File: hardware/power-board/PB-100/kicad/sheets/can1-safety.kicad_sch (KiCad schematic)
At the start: 2 parts

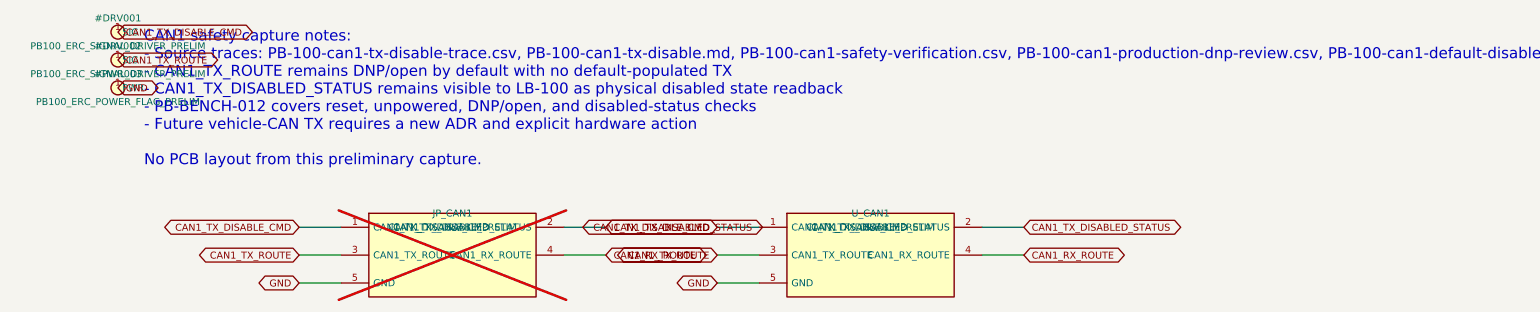
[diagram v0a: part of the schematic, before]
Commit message: Remediate PB footprint pad mapping
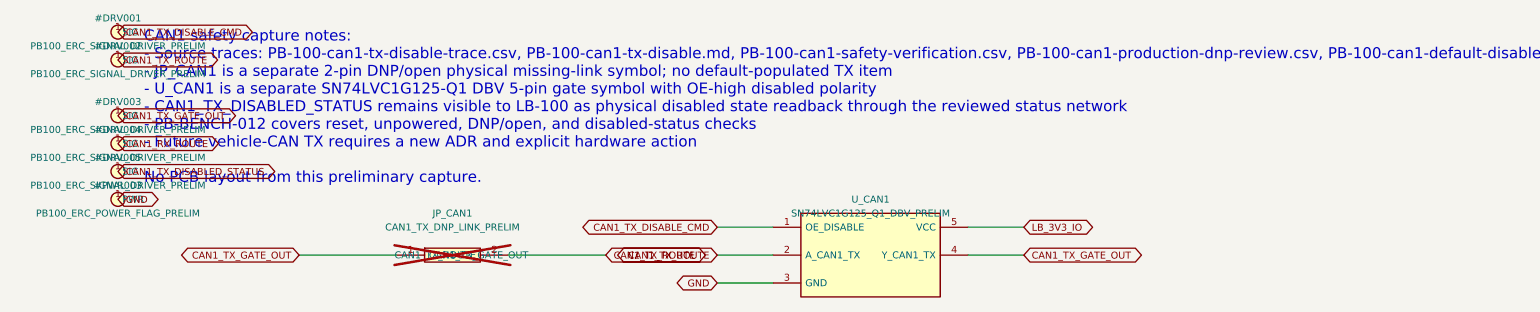
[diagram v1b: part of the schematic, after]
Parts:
- JP_CAN1: value CAN1_TX_DISABLE_PRELIM -> CAN1_TX_DNP_LINK_PRELIM; symbol PB100:PB100_CAN1_TX_DISABLE_PRELIM -> PB100:PB100_CAN1_TX_DNP_LINK_PRELIM
- U_CAN1: value CAN1_TX_DISABLE_PRELIM -> SN74LVC1G125_Q1_DBV_PRELIM; symbol PB100:PB100_CAN1_TX_DISABLE_PRELIM -> PB100:PB100_SN74LVC1G125_Q1_DBV_PRELIM
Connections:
- net CAN1_RX_ROUTE: no longer JP_CAN1.4 (CAN1_RX_ROUTE), U_CAN1.4 (CAN1_RX_ROUTE)
- net CAN1_TX_DISABLED_STATUS: no longer JP_CAN1.2 (CAN1_TX_DISABLED_STATUS), U_CAN1.2 (CAN1_TX_DISABLED_STATUS)
- net CAN1_TX_DISABLE_CMD: no longer JP_CAN1.1 (CAN1_TX_DISABLE_CMD)
- net CAN1_TX_ROUTE: now also JP_CAN1.2 (CAN1_TX_ROUTE), U_CAN1.2 (A_CAN1_TX); no longer JP_CAN1.3 (CAN1_TX_ROUTE), U_CAN1.3 (CAN1_TX_ROUTE)
- net GND: now also U_CAN1.3 (GND); no longer JP_CAN1.5 (GND), U_CAN1.5 (GND)
- new net CAN1_TX_GATE_OUT: JP_CAN1.1 (CAN1_TX_GATE_OUT), U_CAN1.4 (Y_CAN1_TX)
- new net LB_3V3_IO: U_CAN1.5 (VCC)

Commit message: fix
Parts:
- added R_CAN1_OE, R_CAN1_TX_BIAS: 47k 1%, PB100:R0402, symbol PB100:PB100_CAN1_SAFETY_RESISTOR_PRELIM
- added R_CAN1_STATUS_PULL: 100k 1%, PB100:R0402, symbol PB100:PB100_CAN1_SAFETY_RESISTOR_PRELIM
- added R_CAN1_STATUS_SER: 1k 1%, PB100:R0402, symbol PB100:PB100_CAN1_SAFETY_RESISTOR_PRELIM
- JP_CAN1: footprint (none) -> PB100:R0603_DNP_LINK_1608Metric
- U_CAN1: footprint (none) -> PB100:SOT-23-5_DBV_TI
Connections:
- net CAN1_TX_DISABLED_STATUS: now also R_CAN1_STATUS_PULL.2 (B), R_CAN1_STATUS_SER.2 (B)
- net CAN1_TX_DISABLE_CMD: now also R_CAN1_OE.2 (B), R_CAN1_STATUS_SER.1 (A)
- net CAN1_TX_ROUTE: no longer JP_CAN1.2 (CAN1_TX_ROUTE)
- net LB_3V3_IO: now also R_CAN1_OE.1 (A), R_CAN1_STATUS_PULL.1 (A), R_CAN1_TX_BIAS.1 (A)
- new net CAN1_TXD_SAFE: JP_CAN1.2 (CAN1_TXD_SAFE), R_CAN1_TX_BIAS.2 (B)
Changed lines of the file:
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@@
     (property "Reference" "JP_CAN1" (at 76.20 53.34 0) (effects (font (size 1.27 1.27))))
     (property "Value" "CAN1_TX_DNP_LINK_PRELIM" (at 76.20 55.88 0) (effects (font (size 1.27 1.27))))
-    (property "Footprint" "" (at 76.20 66.04 0) (effects (font (size 1.27 1.27)) hide))
+    (property "Footprint" "PB100:R0603_DNP_LINK_1608Metric" (at 76.20 66.04 0) (effects (font (size 1.27 1.27)) hide))
     (property "Datasheet" "../PB-100-can1-tx-disable.md" (at 76.20 68.58 0) (effects (font (size 1.27 1.27)) hide))
     (pin "1")
@@
   (global_label "CAN1_TX_GATE_OUT" (shape bidirectional) (at 48.26 60.96 0) (fields_autoplaced) (effects (font (size 1.27 1.27)) (justify right)) (property "Intersheetrefs" "${INTERSHEET_REFS}" (at 48.26 60.96 0) (effects (font (size 1.27 1.27)) hide)))
   (wire (pts (xy 86.36 60.96) (xy 104.14 60.96)) (stroke (width 0) (type default)))
-  (global_label "CAN1_TX_ROUTE" (shape bidirectional) (at 104.14 60.96 0) (fields_autoplaced) (effects (font (size 1.27 1.27)) (justify left)) (property "Intersheetrefs" "${INTERSHEET_REFS}" (at 104.14 60.96 0) (effects (font (size 1.27 1.27)) hide)))
+  (global_label "CAN1_TXD_SAFE" (shape bidirectional) (at 104.14 60.96 0) (fields_autoplaced) (effects (font (size 1.27 1.27)) (justify left)) (property "Intersheetrefs" "${INTERSHEET_REFS}" (at 104.14 60.96 0) (effects (font (size 1.27 1.27)) hide)))
   (symbol
     (lib_id "PB100:PB100_SN74LVC1G125_Q1_DBV_PRELIM")
@@
     (property "Reference" "U_CAN1" (at 152.40 50.80 0) (effects (font (size 1.27 1.27))))
     (property "Value" "SN74LVC1G125_Q1_DBV_PRELIM" (at 152.40 53.34 0) (effects (font (size 1.27 1.27))))
-    (property "Footprint" "" (at 152.40 71.12 0) (effects (font (size 1.27 1.27)) hide))
+    (property "Footprint" "PB100:SOT-23-5_DBV_TI" (at 152.40 71.12 0) (effects (font (size 1.27 1.27)) hide))
     (property "Datasheet" "https://www.ti.com/lit/ds/symlink/sn74lvc1g125-q1.pdf" (at 152.40 73.66 0) (effects (font (size 1.27 1.27)) hide))
     (pin "1")
@@
   (global_label "LB_3V3_IO" (shape bidirectional) (at 180.34 55.88 0) (fields_autoplaced) (effects (font (size 1.27 1.27)) (justify left)) (property "Intersheetrefs" "${INTERSHEET_REFS}" (at 180.34 55.88 0) (effects (font (size 1.27 1.27)) hide)))
   (symbol
+    (lib_id "PB100:PB100_CAN1_SAFETY_RESISTOR_PRELIM")
+    (at 76.20 91.44 0)
+    (unit 1)
+    (exclude_from_sim no)
+    (in_bom yes)
+    (on_board yes)
+    (dnp no)
+    (property "Reference" "R_CAN1_OE" (at 76.20 86.36 0) (effects (font (size 1.27 1.27))))
+    (property "Value" "47k 1%" (at 76.20 88.90 0) (effects (font (size 1.27 1.27))))
+    (property "Footprint" "PB100:R0402" (at 76.20 96.52 0) (effects (font (size 1.27 1.27)) hide))
+    (property "Datasheet" "../PB-100-can1-tx-disable-design-calculation.md" (at 76.20 99.06 0) (effects (font (size 1.27 1.27)) hide))
+    (pin "1")
+    (pin "2")
+    (instances
+      (project "PB-100"
+        (path "/1af68b81-10b0-5461-9124-39421a2a6932/80055f99-6297-4ce2-96ea-d333e2a69a50/"
+          (reference "R_CAN1_OE")
+          (unit 1)
+        )
+      )
+    )
+  )
+  (global_label "LB_3V3_IO" (shape bidirectional) (at 68.58 91.44 0) (fields_autoplaced) (effects (font (size 1.27 1.27)) (justify right)) (property "Intersheetrefs" "${INTERSHEET_REFS}" (at 68.58 91.44 0) (effects (font (size 1.27 1.27)) hide)))
+  (global_label "CAN1_TX_DISABLE_CMD" (shape bidirectional) (at 83.82 91.44 0) (fields_autoplaced) (effects (font (size 1.27 1.27)) (justify left)) (property "Intersheetrefs" "${INTERSHEET_REFS}" (at 83.82 91.44 0) (effects (font (size 1.27 1.27)) hide)))
+  (symbol
+    (lib_id "PB100:PB100_CAN1_SAFETY_RESISTOR_PRELIM")
+    (at 127.00 91.44 0)
+    (unit 1)
+    (exclude_from_sim no)
+    (in_bom yes)
+    (on_board yes)
+    (dnp no)
+    (property "Reference" "R_CAN1_TX_BIAS" (at 127.00 86.36 0) (effects (font (size 1.27 1.27))))
+    (property "Value" "47k 1%" (at 127.00 88.90 0) (effects (font (size 1.27 1.27))))
+    (property "Footprint" "PB100:R0402" (at 127.00 96.52 0) (effects (font (size 1.27 1.27)) hide))
+    (property "Datasheet" "../PB-100-can1-tx-disable-design-calculation.md" (at 127.00 99.06 0) (effects (font (size 1.27 1.27)) hide))
+    (pin "1")
+    (pin "2")
+    (instances
+      (project "PB-100"
+        (path "/1af68b81-10b0-5461-9124-39421a2a6932/8b75beab-22de-42a1-ba89-68e9bd2ad844/"
+          (reference "R_CAN1_TX_BIAS")
+          (unit 1)
+        )
+      )
+    )
+  )
+  (global_label "LB_3V3_IO" (shape bidirectional) (at 119.38 91.44 0) (fields_autoplaced) (effects (font (size 1.27 1.27)) (justify right)) (property "Intersheetrefs" "${INTERSHEET_REFS}" (at 119.38 91.44 0) (effects (font (size 1.27 1.27)) hide)))
+  (global_label "CAN1_TXD_SAFE" (shape bidirectional) (at 134.62 91.44 0) (fields_autoplaced) (effects (font (size 1.27 1.27)) (justify left)) (property "Intersheetrefs" "${INTERSHEET_REFS}" (at 134.62 91.44 0) (effects (font (size 1.27 1.27)) hide)))
+  (symbol
+    (lib_id "PB100:PB100_CAN1_SAFETY_RESISTOR_PRELIM")
+    (at 76.20 116.84 0)
+    (unit 1)
+    (exclude_from_sim no)
+    (in_bom yes)
+    (on_board yes)
+    (dnp no)
+    (property "Reference" "R_CAN1_STATUS_SER" (at 76.20 111.76 0) (effects (font (size 1.27 1.27))))
+    (property "Value" "1k 1%" (at 76.20 114.30 0) (effects (font (size 1.27 1.27))))
+    (property "Footprint" "PB100:R0402" (at 76.20 121.92 0) (effects (font (size 1.27 1.27)) hide))
+    (property "Datasheet" "../PB-100-can1-tx-disable-design-calculation.md" (at 76.20 124.46 0) (effects (font (size 1.27 1.27)) hide))
+    (pin "1")
+    (pin "2")
+    (instances
+      (project "PB-100"
+        (path "/1af68b81-10b0-5461-9124-39421a2a6932/32b2e633-ddfb-4068-9ee8-5caed1060666/"
+          (reference "R_CAN1_STATUS_SER")
+          (unit 1)
+        )
+      )
+    )
+  )
+  (global_label "CAN1_TX_DISABLE_CMD" (shape bidirectional) (at 68.58 116.84 0) (fields_autoplaced) (effects (font (size 1.27 1.27)) (justify right)) (property "Intersheetrefs" "${INTERSHEET_REFS}" (at 68.58 116.84 0) (effects (font (size 1.27 1.27)) hide)))
+  (global_label "CAN1_TX_DISABLED_STATUS" (shape bidirectional) (at 83.82 116.84 0) (fields_autoplaced) (effects (font (size 1.27 1.27)) (justify left)) (property "Intersheetrefs" "${INTERSHEET_REFS}" (at 83.82 116.84 0) (effects (font (size 1.27 1.27)) hide)))
+  (symbol
+    (lib_id "PB100:PB100_CAN1_SAFETY_RESISTOR_PRELIM")
+    (at 127.00 116.84 0)
+    (unit 1)
+    (exclude_from_sim no)
+    (in_bom yes)
+    (on_board yes)
+    (dnp no)
+    (property "Reference" "R_CAN1_STATUS_PULL" (at 127.00 111.76 0) (effects (font (size 1.27 1.27))))
+    (property "Value" "100k 1%" (at 127.00 114.30 0) (effects (font (size 1.27 1.27))))
+    (property "Footprint" "PB100:R0402" (at 127.00 121.92 0) (effects (font (size 1.27 1.27)) hide))
+    (property "Datasheet" "../PB-100-can1-tx-disable-design-calculation.md" (at 127.00 124.46 0) (effects (font (size 1.27 1.27)) hide))
+    (pin "1")
+    (pin "2")
+    (instances
+      (project "PB-100"
+        (path "/1af68b81-10b0-5461-9124-39421a2a6932/ac9557eb-9bb9-41f8-b23a-db6800c089e1/"
+          (reference "R_CAN1_STATUS_PULL")
+          (unit 1)
+        )
+      )
+    )
+  )
+  (global_label "LB_3V3_IO" (shape bidirectional) (at 119.38 116.84 0) (fields_autoplaced) (effects (font (size 1.27 1.27)) (justify right)) (property "Intersheetrefs" "${INTERSHEET_REFS}" (at 119.38 116.84 0) (effects (font (size 1.27 1.27)) hide)))
+  (global_label "CAN1_TX_DISABLED_STATUS" (shape bidirectional) (at 134.62 116.84 0) (fields_autoplaced) (effects (font (size 1.27 1.27)) (justify left)) (property "Intersheetrefs" "${INTERSHEET_REFS}" (at 134.62 116.84 0) (effects (font (size 1.27 1.27)) hide)))
+  (symbol
     (lib_id "PB100:PB100_ERC_SIGNAL_DRIVER_PRELIM")

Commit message: feat(hardware): accept CAN1 and 80V freeze decisions
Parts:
- added C_CAN1_VCC, C_CAN1_VIO: 100nF 50V X7R, PB100:C0402, symbol PB100:PB100_CAN1_DECOUPLING_CAP
- added D_CAN1: ESD2CANFD24QDBZRQ1, PB100:SOT-23-3_DBZ_TI, symbol PB100:PB100_ESD2CANFD24_Q1_PRELIM
- added JP_CAN1_NORMAL: CAN1_NORMAL_MODE_DNP, PB100:R0603_DNP_LINK_1608Metric, symbol PB100:PB100_CAN1_TX_DNP_LINK_PRELIM
- added R_CAN1_SILENT: 47k 1%, PB100:R0402, symbol PB100:PB100_CAN1_SAFETY_RESISTOR_PRELIM
- added R_CAN1_TERM: 120R 1% DNP, PB100:R0603_DNP_LINK_1608Metric, symbol PB100:PB100_CAN1_SAFETY_RESISTOR_PRELIM
- added U_CAN1_PHY: TJA1051TK/3/1J, PB100:HVSON-8_L3.0-W3.0-P0.65-BL-EP, symbol PB100:PB100_TJA1051TK3_CAN_PHY_PRELIM
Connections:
- net CAN1_RX_ROUTE: now also U_CAN1_PHY.4 (RXD)
- net CAN1_TXD_SAFE: now also U_CAN1_PHY.1 (TXD)
- net GND: now also C_CAN1_VCC.2 (B), C_CAN1_VIO.2 (B), D_CAN1.3 (GND), JP_CAN1_NORMAL.2 (CAN1_TXD_SAFE), U_CAN1_PHY.2 (GND), U_CAN1_PHY.9 (EP_GND)
- net LB_3V3_IO: now also C_CAN1_VIO.1 (A), R_CAN1_SILENT.1 (A), U_CAN1_PHY.5 (VIO)
- new net CAN1_HARNESS_H: D_CAN1.1 (LINE1_CANH), R_CAN1_TERM.1 (A), U_CAN1_PHY.7 (CANH)
- new net CAN1_HARNESS_L: D_CAN1.2 (LINE2_CANL), R_CAN1_TERM.2 (B), U_CAN1_PHY.6 (CANL)
- new net CAN1_PHY_SILENT: JP_CAN1_NORMAL.1 (CAN1_TX_GATE_OUT), R_CAN1_SILENT.2 (B), U_CAN1_PHY.8 (S_SILENT)
- new net PB_5V_OUT: C_CAN1_VCC.1 (A), U_CAN1_PHY.3 (VCC)
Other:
- note added: "CAN1 safety and physical-layer notes: - Sources: PB-100-can1-production-dnp-review.csv and PB-100-can1-reset-bench-checklist.csv - ADR-0015 candidate A is Accepted: PB-100 owns transceiver, ESD, optional termination, CANH/CANL and harness boundary; LB-100 owns FDCAN, protocol and read-only firmware policy - Mandatory TX chain: CAN1_TX_ROUTE -> U_CAN1 -> CAN1_TX_GATE_OUT -> JP_CAN1 DNP/open -> CAN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"
- note removed: "CAN1 safety capture notes: - Source traces: PB-100-can1-tx-disable-trace.csv, PB-100-can1-tx-disable.md, PB-100-can1-safety-verification.csv, PB-100-can1-production-dnp-review.csv, PB-100-can1-default-disable-freeze-checklist.csv, PB-100-can1-default-disable-derivation-precheck.csv, PB-100-can1-default-disable-closeout-precheck.csv, PB-100-can1-reset-bench-checklist.csv, PB-100-schematic-net-doma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"
